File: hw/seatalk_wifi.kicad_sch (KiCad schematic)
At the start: 42 parts

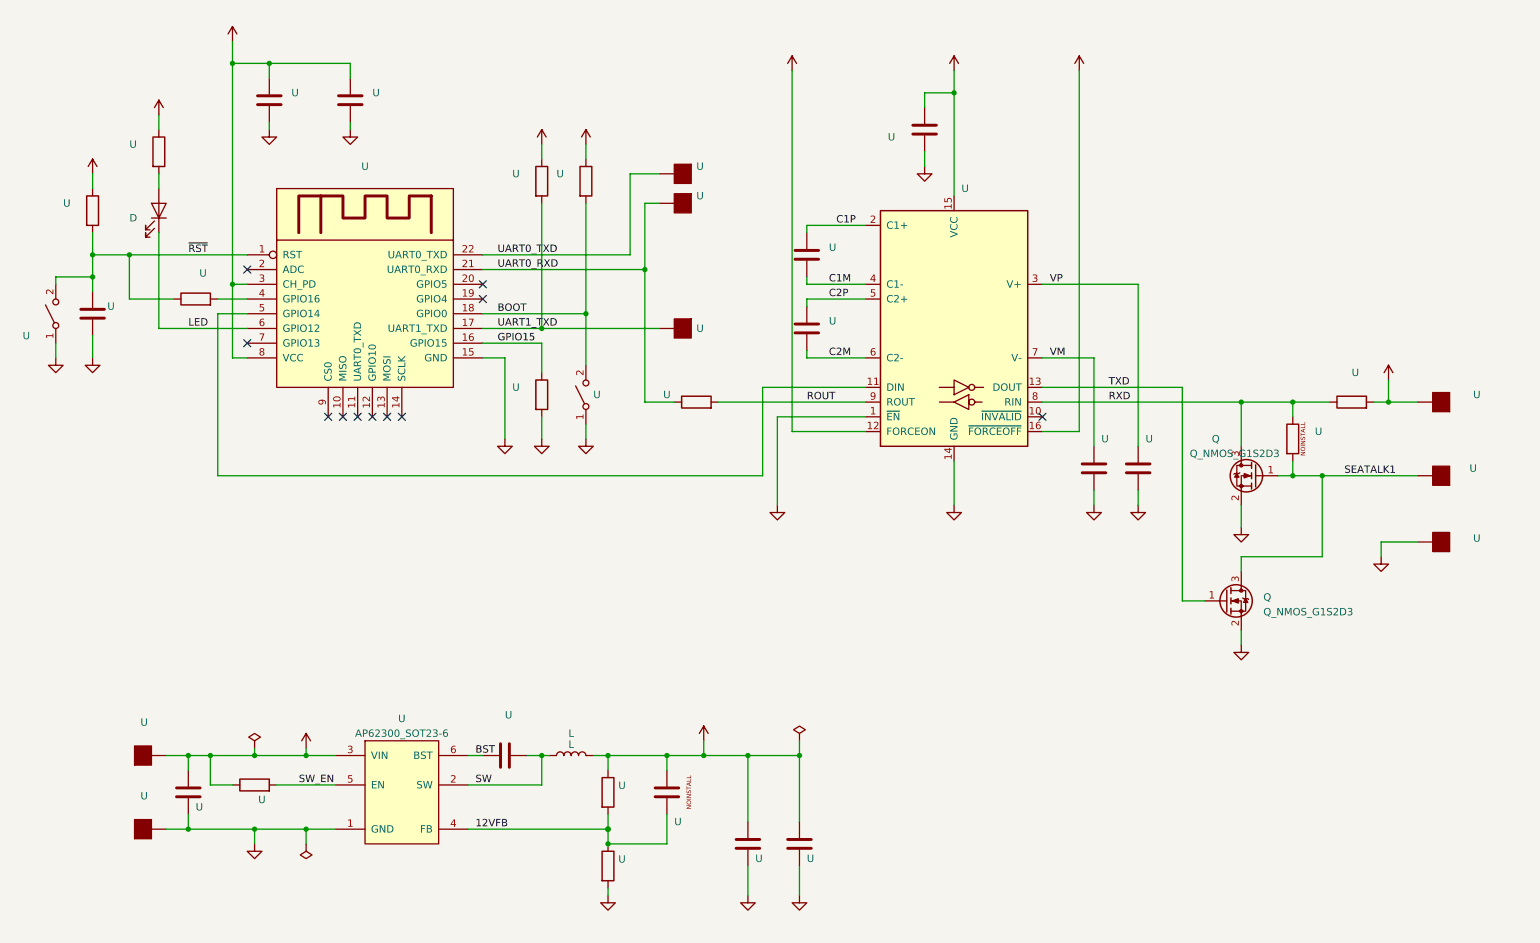
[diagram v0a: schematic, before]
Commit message: Schematic chenged to reflect the voltage of input caps.
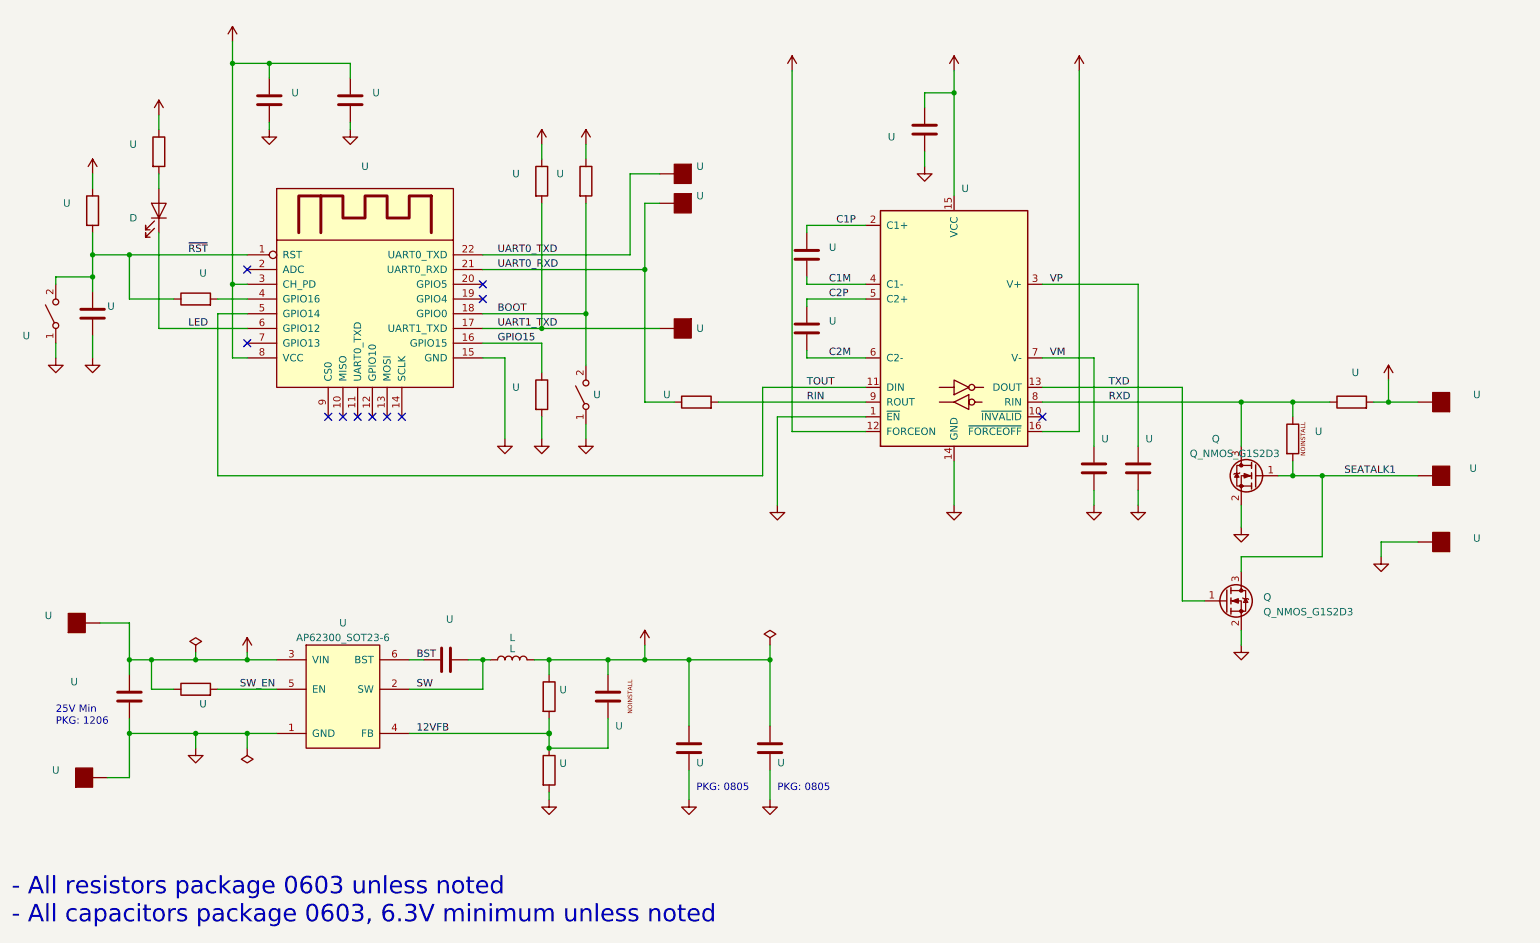
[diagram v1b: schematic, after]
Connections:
- net TOUT: now reaches U.11 (DIN), U.5 (GPIO14)
- net ROUT renamed RIN
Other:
- note added: "- All resistors package 0603 unless noted - All capacitors package 0603, 6.3V minimum unless noted"
- note added: "25V Min PKG: 1206"
- note added: "PKG: 0805"
- title: (none) -> SeaTalk_WiFI
- moved on the sheet: L, U

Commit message: Improvements to web page. SignalK integration. New holder design.
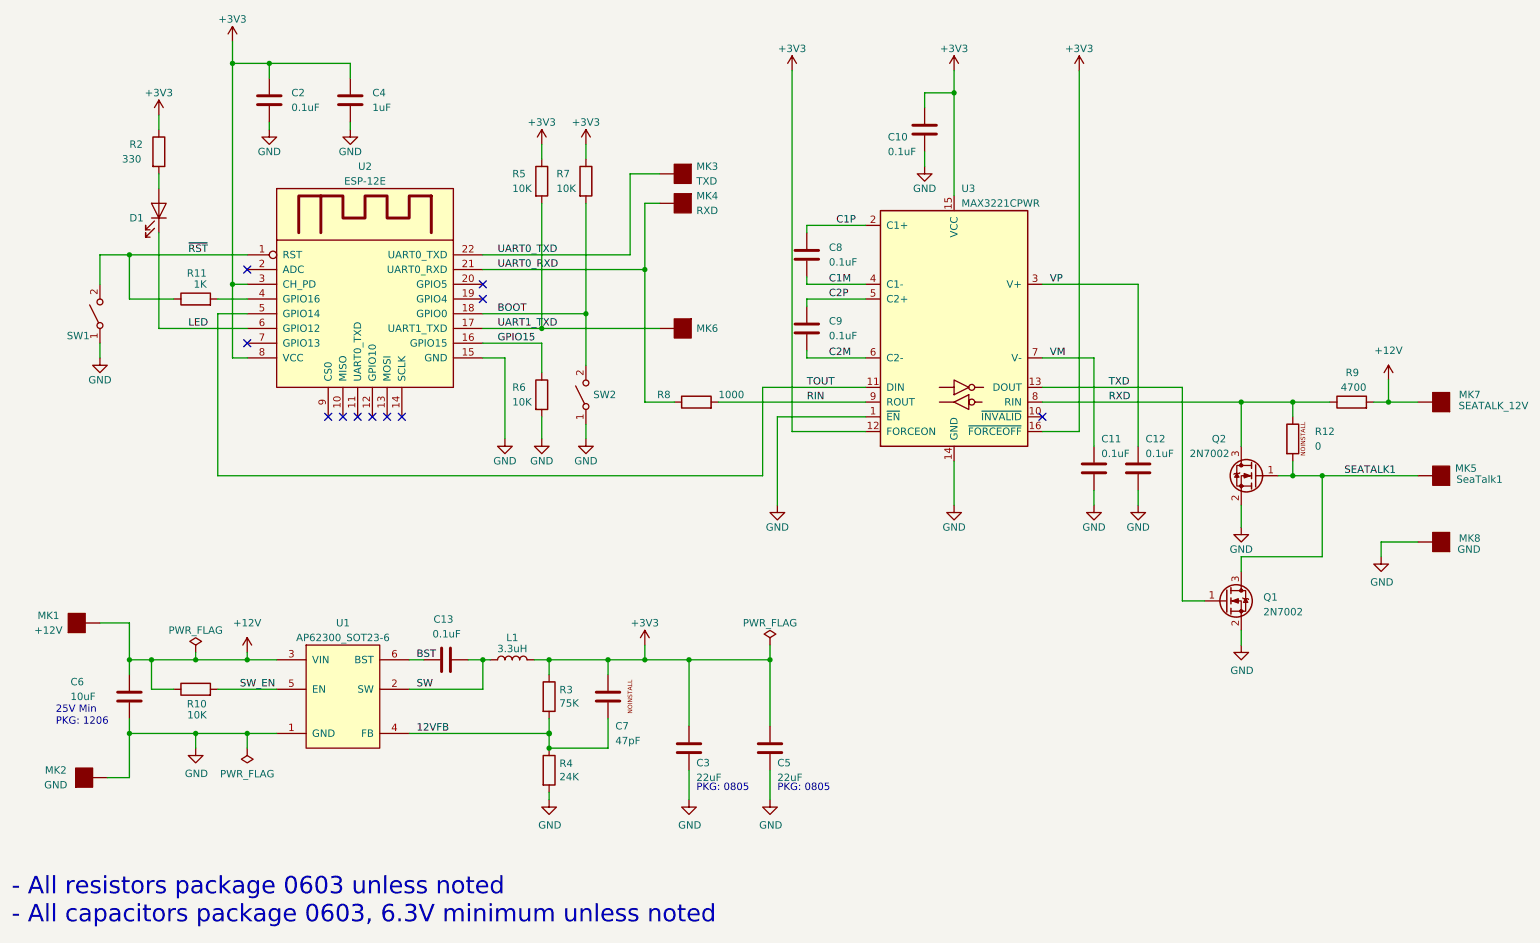
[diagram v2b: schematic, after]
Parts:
- removed U: (no value), symbol device:C
- removed U: (no value), symbol device:R
- C10, C11, C12, C13, C2, C8, C9: renamed from U; value (none) -> 0.1uF; footprint (none) -> capacitor_SMD:C_0603_1608Metric
- C3, C5: renamed from U; value (none) -> 22uF; footprint (none) -> capacitor_SMD:C_0805_2012Metric
- C4: renamed from U; value (none) -> 1uF; footprint (none) -> capacitor_SMD:C_0603_1608Metric
- C6: renamed from U; value (none) -> 10uF; footprint (none) -> capacitor_SMD:C_1206_3216Metric
- C7: renamed from U; value (none) -> 47pF; footprint (none) -> capacitor_SMD:C_0603_1608Metric
- D1: renamed from D; footprint (none) -> led_SMD:LED_0603_1608Metric
- L1: renamed from L; value L -> 3.3uH; footprint (none) -> bourns:INDC3225X120N
- MK1: renamed from U; value (none) -> +12V; footprint (none) -> test_point:TestPoint_Pad_3.0x3.0mm
- MK2, MK8: renamed from U; value (none) -> GND; footprint (none) -> test_point:TestPoint_Pad_3.0x3.0mm
- MK3: renamed from U; value (none) -> TXD; footprint (none) -> test_point:TestPoint_Pad_2.0x2.0mm
- MK4: renamed from U; value (none) -> RXD; footprint (none) -> test_point:TestPoint_Pad_2.0x2.0mm
- MK5: renamed from U; value (none) -> SeaTalk1; footprint (none) -> test_point:TestPoint_Pad_3.0x3.0mm
- MK6: renamed from U; value (none) -> UART1; footprint (none) -> test_point:TestPoint_Pad_2.0x2.0mm
- MK7: renamed from U; value (none) -> SEATALK_12V; footprint (none) -> test_point:TestPoint_Pad_3.0x3.0mm
- Q1, Q2: renamed from Q; value Q_NMOS_G1S2D3 -> 2N7002; footprint (none) -> package_TO_SOT_SMD:SOT23-3
- R10, R5, R6, R7: renamed from U; value (none) -> 10K; footprint (none) -> resistor_SMD:R_0603_1608Metric
- R11: renamed from U; value (none) -> 1K; footprint (none) -> resistor_SMD:R_0603_1608Metric
- R12: renamed from U; value (none) -> 0; footprint (none) -> resistor_SMD:R_0603_1608Metric
- R2: renamed from U; value (none) -> 330; footprint (none) -> resistor_SMD:R_0603_1608Metric
- R3: renamed from U; value (none) -> 75K; footprint (none) -> resistor_SMD:R_0603_1608Metric
- R4: renamed from U; value (none) -> 24K; footprint (none) -> resistor_SMD:R_0603_1608Metric
- R8: renamed from U; value (none) -> 1000; footprint (none) -> resistor_SMD:R_0603_1608Metric
- R9: renamed from U; value (none) -> 4700; footprint (none) -> resistor_SMD:R_0603_1608Metric
- SW1, SW2: renamed from U; value (none) -> SW_SPST; footprint (none) -> apem:ADTSM31NV
- U2: renamed from U; value (none) -> ESP-12E; footprint (none) -> espressif:ESP-12E
- U3: renamed from U; value (none) -> MAX3221CPWR; footprint (none) -> package_SO:TSSOP-16_4.4x5mm_P0.65mm
- renumbered U to U1
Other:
- moved on the sheet: SW1
